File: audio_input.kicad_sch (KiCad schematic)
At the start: 12 parts, among them J5 extra_input, J6 AudioJack4

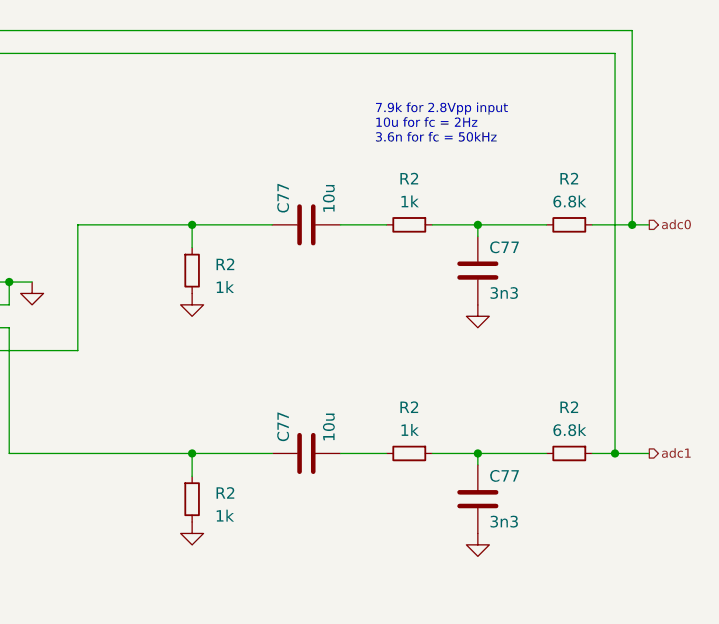
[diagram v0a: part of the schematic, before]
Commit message: update to kicad 8
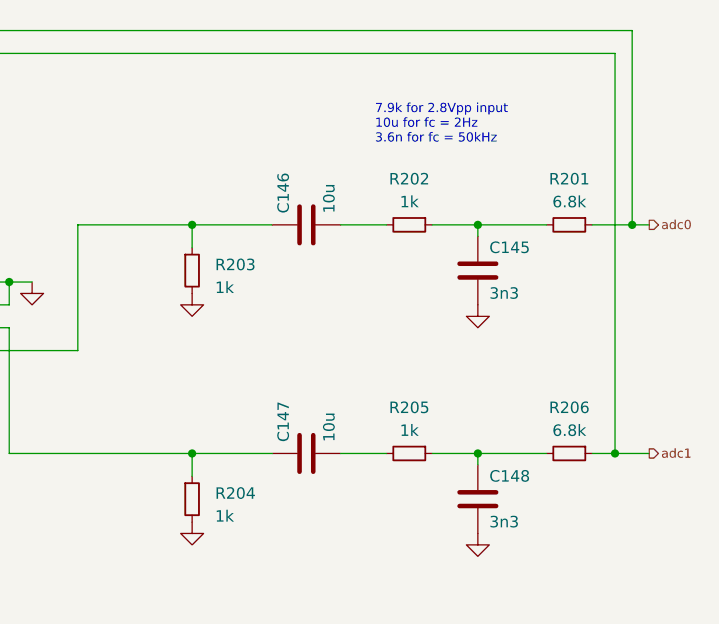
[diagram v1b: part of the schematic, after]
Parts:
- renumbered C77 to C145, C77 to C146, C77 to C147, C77 to C148, R2 to R201, R2 to R202, R2 to R203, R2 to R204, R2 to R205, R2 to R206

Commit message: updates
* add line out
* fix almost all erc
* some more random edits
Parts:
- added D21, D22: 5V, symbol Device:D_TVS
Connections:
- net GND: now also D21.1 (A1), D22.1 (A1)
- net at C147.1, J6.R1, R204.1: now also D22.2 (A2)
- net at C146.1, J6.T, R203.1: now also D21.2 (A2)

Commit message: add power input +...
+ tons of fixes, footprint assignments, etc
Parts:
- D21, D22: footprint (none) -> invendelirium_general:D_SOD-523_bidi

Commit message: fill in some part numbers
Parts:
- R201, R206: PN (none) -> RT0603DRE076K8L
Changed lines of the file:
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@@
+			)
+		)
+		(property "PN" "RT0603DRE076K8L"
+			(at 229.87 54.61 0)
+			(effects
+				(font
+					(size 1.27 1.27)
+				)
+				(hide yes)
 			)
 		)
@@
 			(at 229.87 80.01 0)
 			(effects
+				(font
+					(size 1.27 1.27)
+				)
+				(hide yes)
+			)
+		)
+		(property "PN" "RT0603DRE076K8L"
+			(at 229.87 80.01 0)
+			(effects

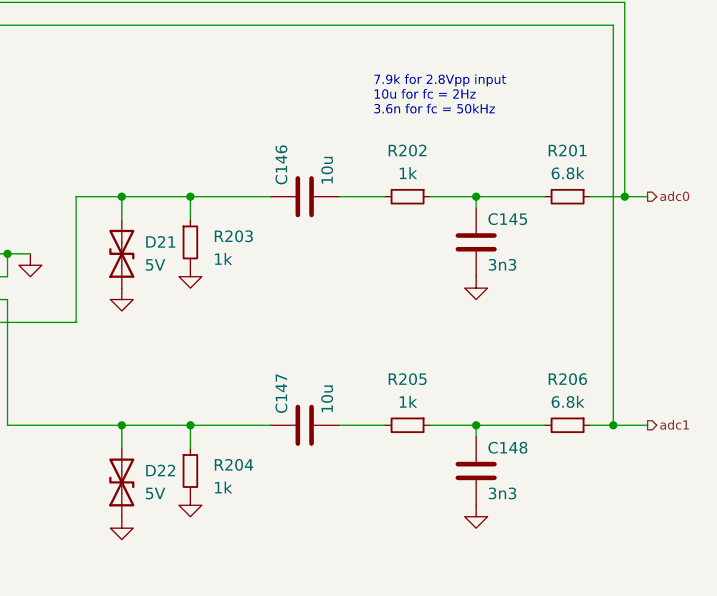
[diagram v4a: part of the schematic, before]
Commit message: update values to what's being used + mark thin film resistors
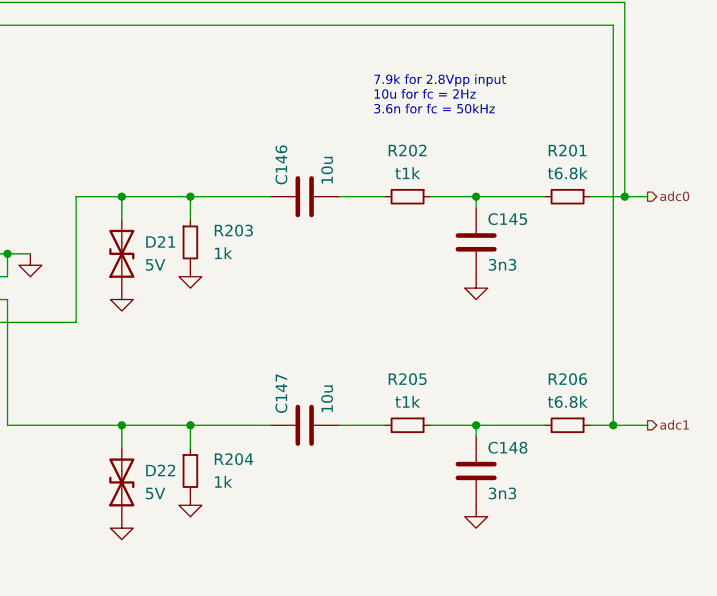
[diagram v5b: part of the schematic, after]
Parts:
- R201, R206: value 6.8k -> t6.8k
- R202, R205: value 1k -> t1k
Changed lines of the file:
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@@
 			)
 		)
-		(property "Value" "6.8k"
+		(property "Value" "t6.8k"
 			(at 229.87 52.07 90)
 			(effects
@@
 		(fields_autoplaced yes)
 		(property "Reference" "R204"
-			(at 190.5 84.455 0)
+			(at 190.5 83.8199 0)
 			(effects
 				(font
@@
 		)
 		(property "Value" "1k"
-			(at 190.5 86.995 0)
+			(at 190.5 86.3599 0)
 			(effects
 				(font
@@
 			)
 		)
-		(property "Value" "1k"
+		(property "Value" "t1k"
 			(at 212.09 52.07 90)
 			(effects
@@
 		(fields_autoplaced yes)
 		(property "Reference" "R203"
-			(at 190.5 59.055 0)
+			(at 190.5 58.4199 0)
 			(effects
 				(font
@@
 		)
 		(property "Value" "1k"
-			(at 190.5 61.595 0)
+			(at 190.5 60.9599 0)
 			(effects
 				(font
@@
 			)
 		)
-		(property "Value" "6.8k"
+		(property "Value" "t6.8k"
 			(at 229.87 77.47 90)
 			(effects
@@
 			)
 		)
-		(property "Value" "1k"
+		(property "Value" "t1k"
 			(at 212.09 77.47 90)
 			(effects

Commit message: work on bugs
* align parts
* enlarge cercaps
* fix ak caps
* improve jack footprint
* fix lmr stencil openings
* remove one ldo
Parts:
- C146, C147: footprint invendelirium_audio:C_0603 -> invendelirium_audio:C_0603_larger
- J6: footprint Connector_Audio:Jack_3.5mm_PJ320D_Horizontal -> invendelirium_audio:Jack_3.5mm_PJ320D_Horizontal
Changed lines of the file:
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@@
 			)
 		)
-		(property "Footprint" "invendelirium_audio:C_0603"
+		(property "Footprint" "invendelirium_audio:C_0603_larger"
 			(at 204.47 79.0448 0)
 			(effects
@@
 			)
 		)
-		(property "Footprint" "invendelirium_audio:C_0603"
+		(property "Footprint" "invendelirium_audio:C_0603_larger"
 			(at 204.47 53.6448 0)
 			(effects
@@
 			)
 		)
-		(property "Footprint" "Connector_Audio:Jack_3.5mm_PJ320D_Horizontal"
+		(property "Footprint" "invendelirium_audio:Jack_3.5mm_PJ320D_Horizontal"
 			(at 158.75 63.5 0)
 			(effects

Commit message: all known bugs fixed
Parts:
- removed J5: extra_input, Connector_JST:JST_GH_BM05B-GHS-TBT_1x05-1MP_P1.25mm_Vertical, symbol Connector_Generic:Conn_01x05
- added J12: Conn_01x06, Connector_JST:JST_GH_BM06B-GHS-TBT_1x06-1MP_P1.25mm_Vertical, symbol Connector_Generic:Conn_01x06
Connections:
- net 5V: now also J12.1 (Pin_1)
- net GND: now also J12.6 (Pin_6)
- net adc0: now also J12.3 (Pin_3)
- net adc1: now also J12.4 (Pin_4)
- net fakegnd: now also J12.5 (Pin_5)
- new net -5V: J12.2 (Pin_2)

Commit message: more bom updates
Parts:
- C145, C148: value 3n3 -> 3.3n
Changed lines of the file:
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@@
 			)
 		)
-		(property "Value" "3n3"
+		(property "Value" "3.3n"
 			(at 220.98 62.23 0)
 			(effects
@@
 			)
 		)
-		(property "Value" "3n3"
+		(property "Value" "3.3n"
 			(at 220.98 87.63 0)
 			(effects
